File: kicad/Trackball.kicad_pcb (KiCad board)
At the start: 2 copper layers, 60 x 55 mm, 49 parts, among them J1 Conn_01x04, J101 Conn_02x03_Counter_Clockwise, J2 Conn_02x04_Counter_Clockwise, SW1 Push_Button, SW101 Push_Button, SW102 Push_Button, SW103 Push_Button, SW104 Push_Button, SW106 Push_Button, SW2 Push_Button, SW3 RotaryEncoder_Switch_MP, U1 ESP32-S3-WROOM-1, U103 TCR2EF19, U2 PMW3360, U4 TLV73333PDBV

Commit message: changement empreinte bouton en\gpio0
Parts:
- SW103, SW106: footprint Button_Switch_SMD:SW_Push_1P1T_NO_CK_KSC7xxJ -> Button_Switch_SMD:SW_SPST_CK_RS282G05A3
- moved SW103 1.80 mm to (96.2, 32.6), turned to 90 degrees
- moved SW106 1.30 mm to (96.8, 32.8)
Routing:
- net EN: track 62.1 -> 55.3 mm
- net GPIO0: track 79.4 -> 74.2 mm

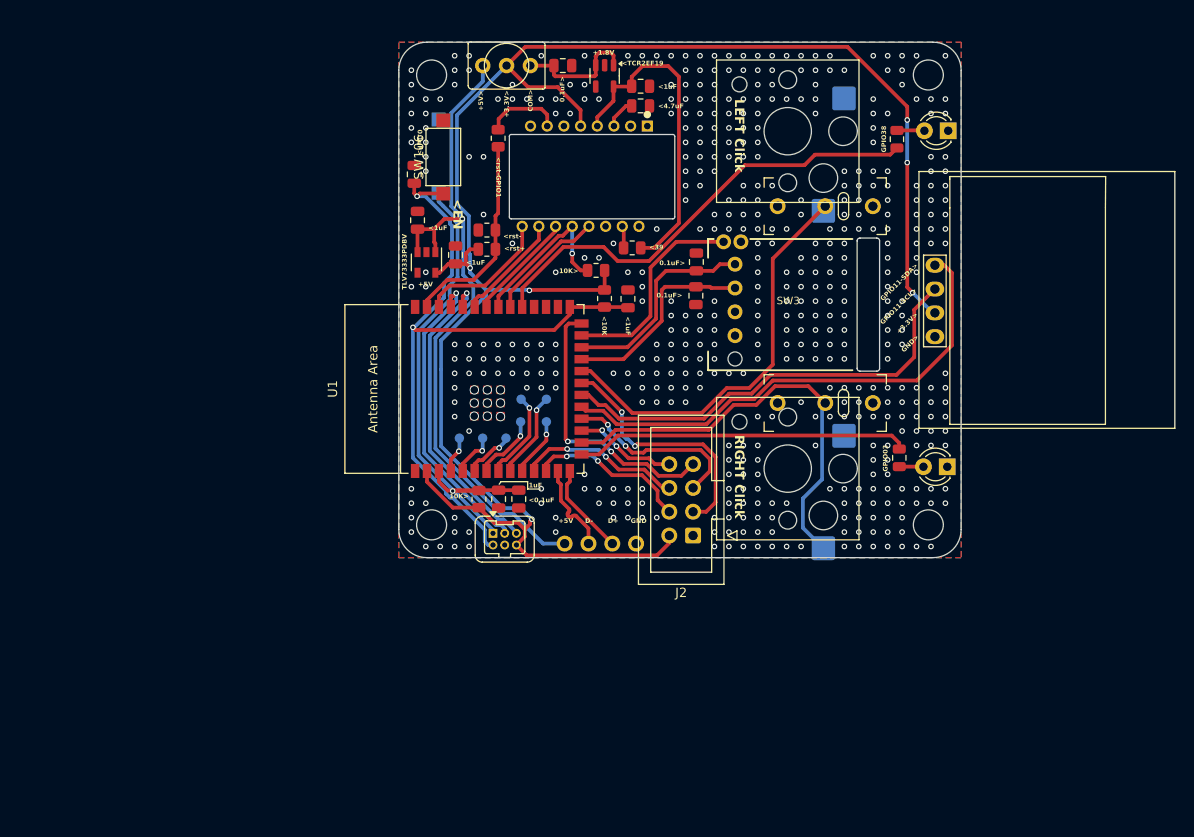
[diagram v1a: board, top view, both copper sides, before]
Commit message: Passage a une molette standard et ajout circuit TP4056
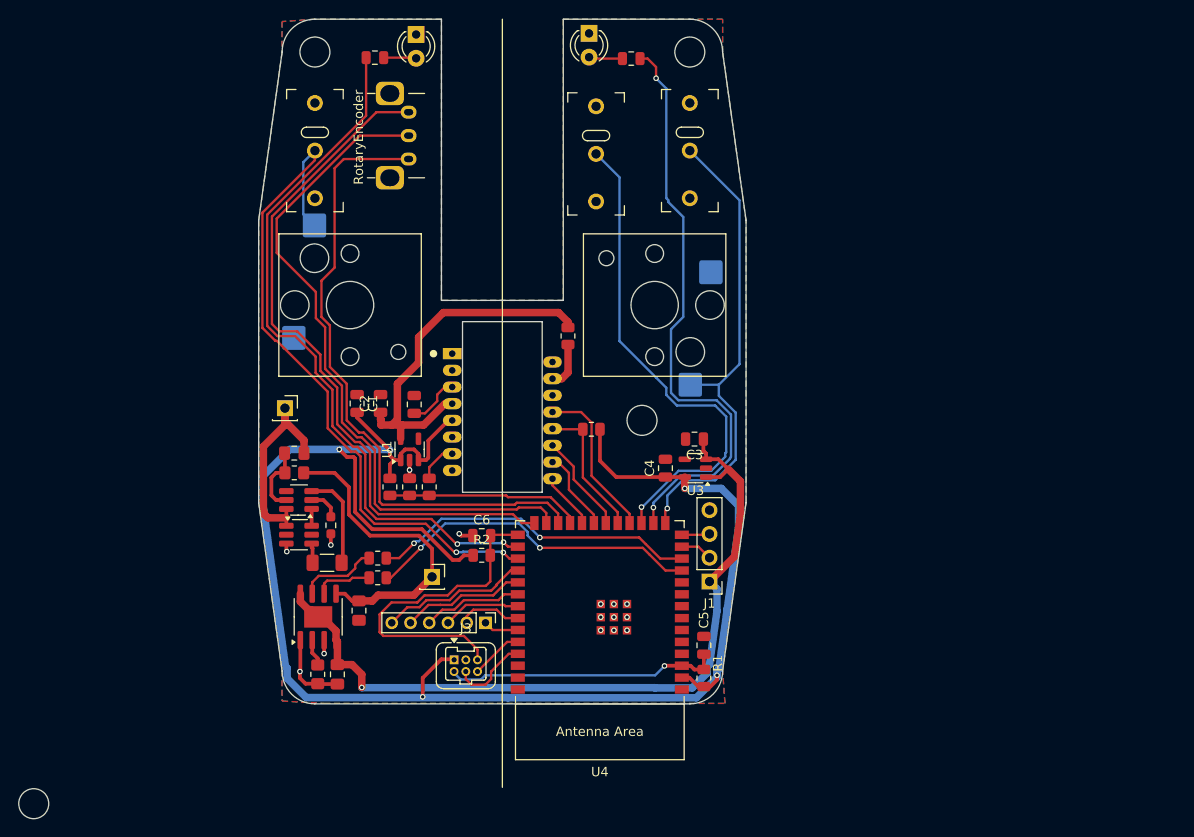
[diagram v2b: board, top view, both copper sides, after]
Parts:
- removed Brd101: SSD1306, SSD1306:128x64OLED
- removed C101, C102, C106, C108, C110: 0.1u, Capacitor_SMD:C_0805_2012Metric
- removed C103, C105, C107, C109, C111: 1u, Capacitor_SMD:C_0805_2012Metric
- removed J101: Conn_02x03_Counter_Clockwise, Connector_Harwin:Harwin_Gecko-G125-FVX0605L0X_2x03_P1.25mm_Vertical
- removed J2: Conn_02x04_Counter_Clockwise, Connector_IDC:IDC-Header_2x04_P2.54mm_Vertical
- removed R103, R104: 10k, Resistor_SMD:R_0805_2012Metric
- removed SW102: Push_Button, PCM_4ms_Switch:Switch_Toggle_SPDT_SubMini
- removed SW103, SW106: Push_Button, Button_Switch_SMD:SW_SPST_CK_RS282G05A3
- removed TP101, TP102, TP103, TP104, TP105, TP106, TP107: TestPoint, TestPoint:TestPoint_Pad_D1.0mm
- removed U103: TCR2EF19, Package_TO_SOT_SMD:SOT-23-5
- added C1: 0.1u, Capacitor_SMD:C_0805_2012Metric, F.Cu at (87.5, 59.0)
- added C2: 1u, Capacitor_SMD:C_0805_2012Metric, F.Cu at (90.0, 59.0)
- added C3: 1u, Capacitor_SMD:C_0805_2012Metric, F.Cu at (123.5, 62.9)
- added C4: 1u, Capacitor_SMD:C_0805_2012Metric, F.Cu at (120.5, 66.0)
- added C5: 0.1u, Capacitor_SMD:C_0805_2012Metric, F.Cu at (124.5, 84.8)
- added C6: 0.1u, Capacitor_SMD:C_0805_2012Metric, F.Cu at (100.8, 73.2)
- added C7: 0.1uF, Capacitor_SMD:C_0805_2012Metric_Pad1.18x1.45mm_HandSolder, F.Cu at (85.5, 88.0)
- added C8: 10uF, Capacitor_SMD:C_0805_2012Metric_Pad1.18x1.45mm_HandSolder, F.Cu at (87.8, 81.2)
- added C9: 0.1uF, Capacitor_SMD:C_0805_2012Metric_Pad1.18x1.45mm_HandSolder, F.Cu at (80.8, 64.3)
- added J10: Conn_01x01_Female, Connector_PinSocket_2.54mm:PinSocket_1x01_P2.54mm_Vertical, F.Cu at (95.5, 77.5)
- added J3: Conn_02x03_Odd_Even, Connector_Harwin:Harwin_Gecko-G125-FVX0605L0X_2x03_P1.25mm_Vertical, F.Cu at (97.9, 86.4)
- added J4: Conn_01x06_Pin, Connector_PinHeader_2.00mm:PinHeader_1x06_P2.00mm_Vertical, F.Cu at (101.3, 82.5)
- added J7: Conn_01x01_Female, Connector_PinSocket_2.54mm:PinSocket_1x01_P2.54mm_Vertical, F.Cu at (79.8, 59.5)
- added R1: 10k, Resistor_SMD:R_0805_2012Metric, F.Cu at (124.5, 88.3)
- added R2: 10k, Resistor_SMD:R_0805_2012Metric, F.Cu at (100.8, 75.2)
- added R3: 1k, Resistor_SMD:R_0805_2012Metric, F.Cu at (89.8, 75.5)
- added R4: 1k, Resistor_SMD:R_0805_2012Metric, F.Cu at (89.8, 77.7)
- added R5: 10k, Resistor_SMD:R_0805_2012Metric_Pad1.20x1.40mm_HandSolder, F.Cu at (83.3, 88.0)
- added R6: 1k, Resistor_SMD:R_0603_1608Metric_Pad0.98x0.95mm_HandSolder, F.Cu at (84.8, 72.0)
- added R7: 0R, Resistor_SMD:R_1206_3216Metric_Pad1.30x1.75mm_HandSolder, F.Cu at (84.3, 76.0)
- added R8: 100, Resistor_SMD:R_0805_2012Metric_Pad1.20x1.40mm_HandSolder, F.Cu at (80.8, 66.5)
- added SW4: Push_Button, MaSe:SW_Micro_Switch, F.Cu at (113.0, 32.4)
- added U3: TLV73333PDBV, Package_TO_SOT_SMD:SOT-23-5, F.Cu at (123.7, 66.0)
- added U5: TP4056, Package_SO:SOIC-8-1EP_3.9x4.9mm_P1.27mm_EP2.29x3mm, F.Cu at (83.4, 81.8)
- added U6: DW01, Package_TO_SOT_SMD:SOT-23-6_Handsoldering, F.Cu at (81.3, 69.3)
- added U7: FS8205A, Package_TO_SOT_SMD:SOT-23-6_Handsoldering, F.Cu at (81.3, 73.0)
- SW1, SW2: footprint PCM_Switch_Keyboard_Hotswap_Kailh:SW_Hotswap_Kailh_Choc_V1V2_1.00u -> MaSe:SW_Hotswap_Kailh_Choc_V1V2_1.00u
- SW104: footprint PCM_openinput:SW_Micro_Switch -> MaSe:SW_Micro_Switch
- SW3: value RotaryEncoder_Switch_MP -> RotaryEncoder; footprint PMW3360:RollerEncoder_Panasonic_EVQWGD001 -> MaSe:Alps-EC10E1220501
- U1: value ESP32-S3-WROOM-1 -> TCR2EF19; footprint PCM_Espressif:ESP32-S3-WROOM-1 -> Package_TO_SOT_SMD:SOT-23-5
- U4: value TLV73333PDBV -> ESP32-S3-WROOM-1; footprint Package_TO_SOT_SMD:SOT-23-5 -> PCM_Espressif:ESP32-S3-WROOM-1
- moved H1 88.6 mm to (53.0, 101.8), turned to 90 degrees
- moved H3 65.5 mm to (83.0, 21.6), turned to 90 degrees
- moved D102 60.0 mm to (112.3, 19.6), turned to -90 degrees
- moved D101 57.7 mm to (93.8, 19.7), turned to -90 degrees
- moved H4 56.5 mm to (123.0, 21.6), turned to 90 degrees
- moved R105 56.4 mm to (89.5, 22.1), turned to 180 degrees
- moved SW101 54.8 mm to (83.0, 32.1), turned to -90 degrees
- moved R106 51.3 mm to (116.8, 22.2), turned to 0 degrees
- moved SW1 50.2 mm to (86.8, 48.5), turned to 90 degrees
- moved SW3 44.1 mm to (93.0, 30.5), turned to 90 degrees
- moved U4 41.6 mm to (113.5, 81.3), turned to 180 degrees
- moved C104 40.0 mm to (93.7, 59.1), turned to 90 degrees
- moved R107 37.9 mm to (95.2, 68.0)
- moved U2 32.0 mm to (97.7, 53.7), turned to 0 degrees
- moved SW104 30.6 mm to (123.0, 32.1), turned to -90 degrees
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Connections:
- R105 pad 2: GPIO38 -> LED2
- R106 pad 2: GPIO3 -> LED1
- R107 pad 1: GPIO1 -> Sensor_RST
- R108 pad 2: GPIO1 -> Sensor_RST
- R109 pad 1: GPIO1 -> Sensor_RST
- SW1 pad 2: GPIO14 -> leftClick
- SW101 pad 2: GPIO14 -> leftClick
- SW104 pad 2: GPIO46 -> rightClick
- SW2 pad 2: GPIO46 -> rightClick
- SW3 pad A: GPIO37 -> encA
- SW3 pad B: GPIO21 -> encB
- SW3 pad C: GND -> encC
- U1 pad 1: GND -> +3V3
- U1 pad 2: +3V3 -> GND
- U1 pad 3: EN -> +3V3
- U1 pad 4: GPIO4 -> unconnected-(U1-NC-Pad4)
- U1 pad 5: GPIO5 -> +1V8
- U4 pad 1: +5V -> GND
- U4 pad 2: GND -> +3V3
- U4 pad 3: +5V -> EN
- U4 pad 5: +3V3 -> unconnected-(U4-GPIO5/TOUCH5/ADC1_CH4-Pad5)
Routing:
- net LED2: track 0.00 -> 76.3 mm, vias 0 -> 2
- net encC: track 0.00 -> 74.1 mm
- net leftClick: track 0.00 -> 73.4 mm, vias 0 -> 2
- net encB: track 0.00 -> 72.8 mm
- net encA: track 0.00 -> 68.1 mm
- net LED1: track 0.00 -> 63.0 mm, vias 0 -> 2
- net GPIO11: track 53.7 -> 0.00 mm
- net CenterClick: track 0.00 -> 53.4 mm, vias 0 -> 1
- net rightClick: track 0.00 -> 51.8 mm, vias 0 -> 1
- net GPIO12: track 47.4 -> 0.00 mm
- net GPIO46: track 46.6 -> 0.00 mm
- net GPIO14: track 44.2 -> 0.00 mm
- net GPIO0: track 74.2 -> 35.3 mm, vias 2 -> 0
- net STDBY: track 0.00 -> 36.2 mm, vias 0 -> 2
- net GPIO38: track 49.4 -> 13.2 mm
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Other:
- board size 60 x 55 mm -> 52 x 73 mm
- board text removed: "+1.8V"
- board text removed: "+1.8V>"
- board text removed: "+3.3V"
- board text removed: "+3.3V>"
- board text removed: "+5V"
- board text removed: "+5V>"
- board text removed: "0.1uF>"
- board text removed: "10K>"
- board text removed: "1uF"
- board text removed: "<0.1uF"
- board text removed: "<10K"
- board text removed: "<1uF"
- board text removed: "<39"
- board text removed: "<4.7uF"
- board text removed: "<EN"
- board text removed: "<GPIO0"
- board text removed: "<GPIO04"
- board text removed: "<GPIO05"
- board text removed: "<GPIO06"
- board text removed: "<GPIO07"
- board text removed: "<GPIO10"
- board text removed: "<GPIO13"
- board text removed: "<GPIO14"
- board text removed: "<GPIO15"
- board text removed: "<GPIO16"
- board text removed: "<GPIO17"
- board text removed: "<GPIO45"
- board text removed: "<GPIO46"
- board text removed: "<TCR2EF19"
- board text removed: "<rst+"
- board text removed: "<rst-"
- board text removed: "<rst-GPIO1"
- board text removed: "COM>"
- board text removed: "D+"
- board text removed: "D-"
- board text removed: "DIR-GPIO21>"
- board text removed: "DIR-GPIO37>"
- board text removed: "GND"
- board text removed: "GND>"
- board text removed: "GPIO02-Motion>"
- board text removed: "GPIO03"
- board text removed: "GPIO08>"
- board text removed: "GPIO09>"
- board text removed: "GPIO11-SCL>"
- board text removed: "GPIO11-SDA>"
- board text removed: "GPIO18>"
- board text removed: "GPIO38"
- board text removed: "GPIO39-NCS>"
- board text removed: "GPIO40-MISO>"
- board text removed: "GPIO41-MOSI>"
- board text removed: "GPIO42-SCLK>"
- board text removed: "LED>"
- board text removed: "LEFT Click"
- board text removed: "MaSe"
- board text removed: "Push_GPIO25>"
- board text removed: "RIGHT Click"
- board text removed: "TLV73333PDBV"

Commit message: changement de taille
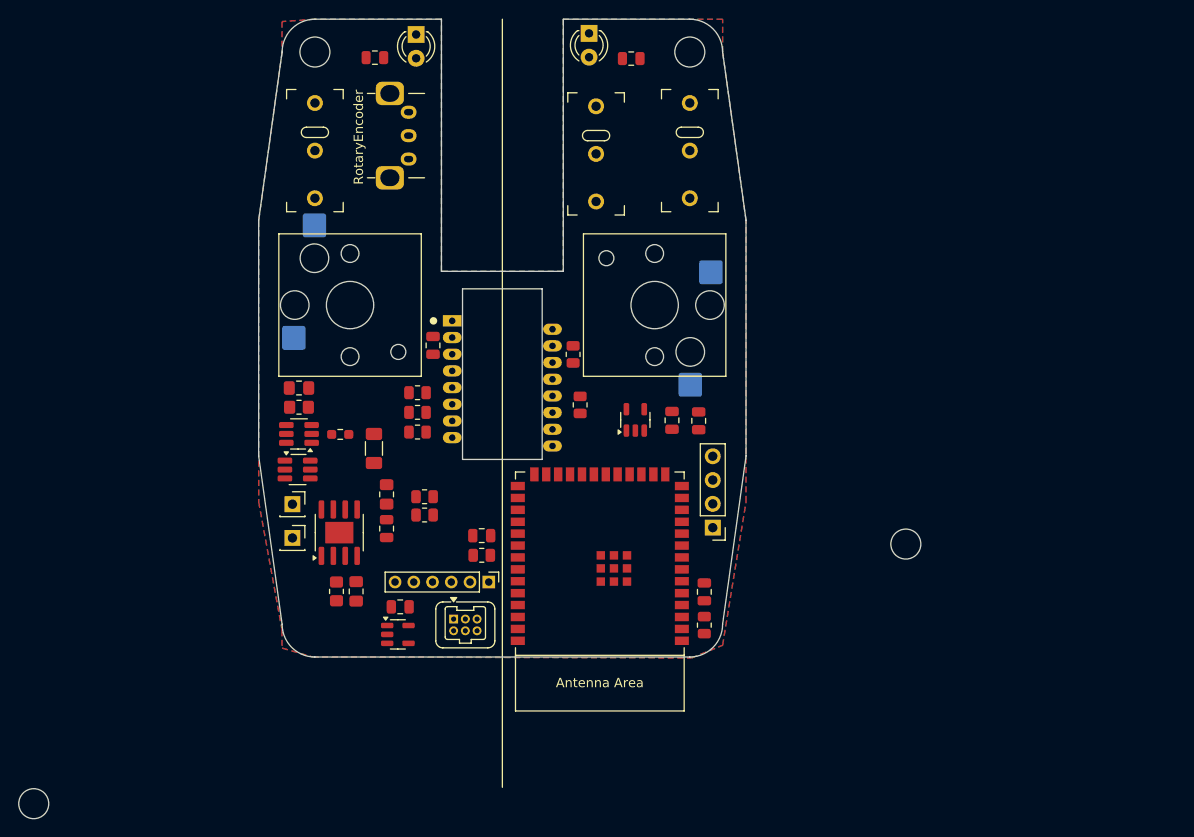
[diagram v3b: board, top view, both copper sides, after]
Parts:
- moved U3 36.4 mm to (91.9, 83.7), turned to 0 degrees
- moved C3 34.2 mm to (90.7, 72.4), turned to -90 degrees
- moved C2 34.0 mm to (124.0, 60.9)
- moved C1 33.6 mm to (121.2, 60.9)
- moved C4 31.9 mm to (92.2, 80.8), turned to 180 degrees
- moved H2 31.1 mm to (146.1, 74.0)
- moved U1 24.3 mm to (117.2, 60.8)
- moved J10 15.5 mm to (80.7, 73.4)
- moved R7 13.2 mm to (89.3, 63.9), turned to -90 degrees
- moved C8 12.7 mm to (90.7, 68.8), turned to 90 degrees
- moved R109 10.5 mm to (94.0, 57.9), turned to 0 degrees
- moved J7 10.3 mm to (80.7, 69.8)
- moved R6 9.75 mm to (85.8, 62.4), turned to 180 degrees
- moved U5 9.27 mm to (85.7, 72.8)
- moved C7 9.07 mm to (87.5, 79.1)
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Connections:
- C3 pad 1: +5V -> BAT+
- U3 pad 1: +5V -> BAT+
- U3 pad 3: +5V -> BAT+
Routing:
- net +3V3: track 177.1 -> 0.00 mm, vias 5 -> 0
- net +5V: track 83.3 -> 0.00 mm, vias 1 -> 0
- net LED2: track 76.3 -> 0.00 mm, vias 2 -> 0
- net encC: track 74.1 -> 0.00 mm
- net leftClick: track 73.4 -> 0.00 mm, vias 2 -> 0
- net encB: track 72.8 -> 0.00 mm
- net encA: track 68.1 -> 0.00 mm
- net LED1: track 63.0 -> 0.00 mm, vias 2 -> 0
- net CenterClick: track 53.4 -> 0.00 mm, vias 1 -> 0
- net rightClick: track 51.8 -> 0.00 mm, vias 1 -> 0
- net +1V8: track 40.0 -> 0.00 mm
- net STDBY: track 36.2 -> 0.00 mm, vias 2 -> 0
- net GPIO0: track 35.3 -> 0.00 mm
- net CHRG: track 35.0 -> 0.00 mm, vias 2 -> 0
- net BAT+: track 33.4 -> 0.00 mm
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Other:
- board size 52 x 73 mm -> 52 x 68 mm

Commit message: repos
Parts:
- removed H1, H2: MountingHole, MountingHole:MountingHole_3.2mm_M3
- removed SW101: Push_Button, PCM_openinput:SW_Micro_Switch
- removed SW104: Push_Button, MaSe:SW_Micro_Switch
- moved R105 37.8 mm to (124.4, 36.4), turned to 0 degrees
- moved D101 32.0 mm to (123.6, 31.5)
- moved R106 14.5 mm to (120.0, 36.4)
- moved D102 13.6 mm to (118.8, 31.5)
- moved C104 7.55 mm to (89.7, 57.5)
- moved H3 6.00 mm to (83.0, 27.6)
- moved R101 5.51 mm to (115.1, 57.0)
- moved H4 4.00 mm to (123.0, 25.6)
- moved SW4 3.92 mm to (113.0, 28.5), turned to 90 degrees
- moved SW1 3.61 mm to (88.8, 45.5)
- moved SW2 3.61 mm to (117.3, 45.5)
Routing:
- net +3V3: track 0.00 -> 129.0 mm, vias 0 -> 6
- net encA: track 0.00 -> 61.7 mm, vias 0 -> 2
- net encB: track 0.00 -> 56.7 mm, vias 0 -> 1
- net LED2: track 0.00 -> 56.3 mm, vias 0 -> 2
- net +5V: track 0.00 -> 53.3 mm, vias 0 -> 1
- net +1V8: track 0.00 -> 52.4 mm, vias 0 -> 2
- net encC: track 0.00 -> 51.4 mm
- net leftClick: track 0.00 -> 48.8 mm, vias 0 -> 3
- net BAT+: track 0.00 -> 48.2 mm, vias 0 -> 2
- net CenterClick: track 0.00 -> 40.6 mm
- net LED1: track 0.00 -> 36.4 mm
- net STDBY: track 0.00 -> 31.1 mm, vias 0 -> 2
- net EN: track 0.00 -> 29.8 mm, vias 0 -> 1
- net GPIO0: track 0.00 -> 29.8 mm, vias 0 -> 2
- net CHRG: track 0.00 -> 27.1 mm, vias 0 -> 2
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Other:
- board size 52 x 68 mm -> 52 x 64 mm

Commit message: next routing try
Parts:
- added H2: MountingHole, MountingHole:MountingHole_3.2mm_M3, F.Cu at (83.0, 82.5)
- moved C2 7.59 mm to (117.3, 57.2), turned to 0 degrees
- moved C6 5.00 mm to (100.9, 68.2)
- moved R2 4.80 mm to (101.0, 70.5)
- moved C104 4.58 mm to (94.0, 55.8), turned to 180 degrees
- moved R101 4.27 mm to (111.2, 55.1)
- moved R7 3.96 mm to (85.5, 62.8)
- moved C8 3.11 mm to (92.0, 71.5), turned to 0 degrees
- moved R3 3.02 mm to (92.1, 67.5)
- moved R4 3.00 mm to (92.1, 69.5)
- moved R108 2.95 mm to (94.0, 63.0)
- moved R5 2.93 mm to (82.7, 78.0), turned to 180 degrees
- moved R6 2.25 mm to (87.7, 63.5), turned to 90 degrees
- moved C3 1.91 mm to (92.1, 73.7), turned to 0 degrees
- moved R107 1.15 mm to (94.0, 61.0)
- moved R102 1.10 mm to (112.5, 59.1)
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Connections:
- net Net-(U5-PROG) renamed /PROG_TP40
- net Net-(U6-CS) renamed /CS_DW01
- net Net-(U6-VCC) renamed /VCC_DW01
- U4 pad 10: unconnected-(U4-GPIO17/U1TXD/ADC2_CH6-Pad10) -> CenterClick
- U4 pad 16: LED1 -> unconnected-(U4-GPIO46-Pad16)
- U4 pad 17: CenterClick -> unconnected-(U4-GPIO9/TOUCH9/ADC1_CH8/FSPIHD/SUBSPIHD-Pad17)
- U4 pad 28: LED2 -> unconnected-(U4-SPIIO6/GPIO35/FSPID/SUBSPID-Pad28)
- U4 pad 8: unconnected-(U4-GPIO15/U0RTS/ADC2_CH4/XTAL_32K_P-Pad8) -> LED2
- U4 pad 9: unconnected-(U4-GPIO16/U0CTS/ADC2_CH5/XTAL_32K_N-Pad9) -> LED1
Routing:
- net +3V3: track 129.0 -> 168.2 mm, vias 6 -> 4
- net GND: track 4.47 -> 21.3 mm, vias 0 -> 724
- net CenterClick: track 40.6 -> 56.5 mm, vias 0 -> 2
- net +5V: track 53.3 -> 68.2 mm
- net LED1: track 36.4 -> 47.5 mm, vias 0 -> 2
- net LED2: track 56.3 -> 46.0 mm
- net encA: track 61.7 -> 52.5 mm
- net +1V8: track 52.4 -> 43.7 mm, vias 2 -> 1
- net BAT-: track 16.2 -> 24.1 mm
- net Net-(U2-VDDPIX): track 11.7 -> 4.07 mm, vias 1 -> 0
- net encC: track 51.4 -> 57.9 mm
- net Net-(U2-LED_P): track 8.33 -> 3.40 mm, vias 1 -> 0
- net CHRG: track 27.1 -> 31.9 mm
- net /OC: track 7.39 -> 2.91 mm
- net GPIO0: track 29.8 -> 34.2 mm, vias 2 -> 0
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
